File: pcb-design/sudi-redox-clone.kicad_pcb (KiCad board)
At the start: 2 copper layers, 204.9 x 155.4 mm, 110 parts, among them J1 RJ12_LEFT, J2 Serial_Out, J3 0.91 OLED, J4 RJ12_RIGHT, K1 KEYSW, K10 KEYSW, K11 KEYSW, K12 KEYSW, K13 KEYSW, K14 KEYSW, K15 KEYSW, K16 KEYSW, K17 KEYSW, K18 KEYSW, K19 KEYSW, K2 KEYSW, K20 KEYSW, K21 KEYSW, K22 KEYSW, K23 KEYSW, K24 KEYSW, K25 KEYSW, K26 KEYSW, K27 KEYSW, K28 KEYSW, K29 KEYSW, K3 KEYSW, K30 KEYSW, K31 KEYSW, K32 KEYSW, K33 KEYSW, K34 KEYSW, K35 KEYSW, K36 KEYSW, K37 KEYSW, K38 KEYSW, K39 KEYSW, K4 KEYSW, K40 KEYSW, K41 KEYSW, K42 KEYSW, K5 KEYSW, K6 KEYSW, K7 KEYSW, K8 KEYSW, K9 KEYSW, U1 ProMicro, U2 MCP23017_SP

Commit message: updatee
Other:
- board text added: "MAKE Front Back MCP23017 MAKE Front Back RJ12 Socket"
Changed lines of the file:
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@@
+		)
+	)
+	(gr_text "MAKE Front Back MCP23017\nMAKE Front Back RJ12 Socket"
+		(at 241 47.5 0)
+		(layer "User.1")
+		(effects
+			(font
+				(size 5 5)
+				(thickness 1.25)
+				(bold yes)
+			)
+			(justify left bottom)
 		)
 	)

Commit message: [minggu 7 juli 12:12] create pcb cut profile
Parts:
- removed D32, D33, D34, D35, D36, D37, D38, D39, D40, D41, D42: 1N5820, canadian_footprints:D_SOD123_axial-dual
- removed K19, K20, K21, K22, K23, K24, K25, K26, K27, K28, K29, K30, K31, K32, K33, K34, K35, K36, K37, K38, K39, K40, K41, K42: KEYSW, canadian_footprints:Mx_Alps_100-dualside
- added AE1: 2.4GHz, RF_Antenna:Texas_SWRA117D_2.4GHz_Left, F.Cu at (65.8, 92.2)
- added AE2: 2.4GHz, RF_Antenna:Texas_SWRA117D_2.4GHz_Left, F.Cu at (-27.0, -81.6)
- added C1: 10uF, Capacitor_SMD:C_0805_2012Metric_Pad1.18x1.45mm_HandSolder, F.Cu at (-52.9, -133.3)
- added C10: 1uF, Capacitor_SMD:C_0805_2012Metric_Pad1.18x1.45mm_HandSolder, F.Cu at (-61.3, -58.9)
- added C11: 100nF, Capacitor_SMD:C_0805_2012Metric_Pad1.18x1.45mm_HandSolder, F.Cu at (-52.9, -121.3)
- added C12: 47nF, Capacitor_SMD:C_0805_2012Metric_Pad1.18x1.45mm_HandSolder, F.Cu at (-52.9, -118.2)
- added C13: 100nF, Capacitor_SMD:C_0805_2012Metric_Pad1.18x1.45mm_HandSolder, F.Cu at (-48.1, -133.3)
- added C14: 1nF, Capacitor_SMD:C_0805_2012Metric_Pad1.18x1.45mm_HandSolder, F.Cu at (-48.1, -130.3)
- added C15: 2.2pF, Capacitor_SMD:C_0805_2012Metric_Pad1.18x1.45mm_HandSolder, F.Cu at (-48.1, -127.3)
- added C16: 1pF, Capacitor_SMD:C_0805_2012Metric_Pad1.18x1.45mm_HandSolder, F.Cu at (-48.1, -124.3)
- added C17: 1.5p, Capacitor_SMD:C_0805_2012Metric_Pad1.18x1.45mm_HandSolder, F.Cu at (-48.1, -121.3)
- added C18: 2.2nF, Capacitor_SMD:C_0805_2012Metric_Pad1.18x1.45mm_HandSolder, F.Cu at (-48.1, -118.2)
- added C19: 12pF, Capacitor_SMD:C_0805_2012Metric_Pad1.18x1.45mm_HandSolder, F.Cu at (-43.3, -133.3)
- added C2: 10uF/5V, Capacitor_SMD:C_0805_2012Metric_Pad1.18x1.45mm_HandSolder, F.Cu at (-52.9, -130.3)
- added C20: 12pF, Capacitor_SMD:C_0805_2012Metric_Pad1.18x1.45mm_HandSolder, F.Cu at (-43.3, -130.3)
- added C21: 100nF, Capacitor_SMD:C_0805_2012Metric_Pad1.18x1.45mm_HandSolder, F.Cu at (-43.3, -127.3)
- added C22: 10uF/5V, Capacitor_SMD:C_0805_2012Metric_Pad1.18x1.45mm_HandSolder, F.Cu at (-61.3, -55.9)
- added C23: 100nF, Capacitor_SMD:C_0805_2012Metric_Pad1.18x1.45mm_HandSolder, F.Cu at (-61.3, -52.9)
- added C24: 1.5p, Capacitor_SMD:C_0805_2012Metric_Pad1.18x1.45mm_HandSolder, F.Cu at (-56.5, -70.9)
- added C25: 1pF, Capacitor_SMD:C_0805_2012Metric_Pad1.18x1.45mm_HandSolder, F.Cu at (-56.5, -67.9)
- added C26: 2.2pF, Capacitor_SMD:C_0805_2012Metric_Pad1.18x1.45mm_HandSolder, F.Cu at (-56.5, -64.9)
- added C27: 2.2nF, Capacitor_SMD:C_0805_2012Metric_Pad1.18x1.45mm_HandSolder, F.Cu at (-56.5, -61.9)
- added C28: 12pF, Capacitor_SMD:C_0805_2012Metric_Pad1.18x1.45mm_HandSolder, F.Cu at (-56.5, -58.9)
- added C29: 12pF, Capacitor_SMD:C_0805_2012Metric_Pad1.18x1.45mm_HandSolder, F.Cu at (-56.5, -55.9)
- added C3: 10uF/5V, Capacitor_SMD:C_0805_2012Metric_Pad1.18x1.45mm_HandSolder, F.Cu at (-52.9, -127.3)
- added C30: 47nF, Capacitor_SMD:C_0805_2012Metric_Pad1.18x1.45mm_HandSolder, F.Cu at (-56.5, -52.9)
- added C31: 100nF, Capacitor_SMD:C_0805_2012Metric_Pad1.18x1.45mm_HandSolder, F.Cu at (-51.7, -70.9)
- added C32: 100nF, Capacitor_SMD:C_0805_2012Metric_Pad1.18x1.45mm_HandSolder, F.Cu at (-51.7, -67.9)
- added C33: 100nF, Capacitor_SMD:C_0805_2012Metric_Pad1.18x1.45mm_HandSolder, F.Cu at (-51.7, -64.9)
- added C34: 1nF, Capacitor_SMD:C_0805_2012Metric_Pad1.18x1.45mm_HandSolder, F.Cu at (-51.7, -61.9)
- added C4: 10uF, Capacitor_SMD:C_0805_2012Metric_Pad1.18x1.45mm_HandSolder, F.Cu at (-52.9, -124.3)
- added C5: 22pF, Capacitor_SMD:C_0805_2012Metric_Pad1.18x1.45mm_HandSolder, F.Cu at (-61.3, -70.9)
- added C6: 22pF, Capacitor_SMD:C_0805_2012Metric_Pad1.18x1.45mm_HandSolder, F.Cu at (-61.3, -67.9)
- added C7: 100nF, Capacitor_SMD:C_0805_2012Metric_Pad1.18x1.45mm_HandSolder, F.Cu at (-61.3, -64.9)
- added C9: 10uF/5V, Capacitor_SMD:C_0805_2012Metric_Pad1.18x1.45mm_HandSolder, F.Cu at (-61.3, -61.9)
- added D43: WS2812B, LED_SMD:LED_WS2812B_PLCC4_5.0x5.0mm_P3.2mm, F.Cu at (-59.5, -131.5)
- added D44: WS2812B, LED_SMD:LED_WS2812B_PLCC4_5.0x5.0mm_P3.2mm, F.Cu at (-59.5, -124.9)
- added D45: WS2812B, LED_SMD:LED_WS2812B_PLCC4_5.0x5.0mm_P3.2mm, F.Cu at (-59.5, -118.3)
- added D46: WS2812B, LED_SMD:LED_WS2812B_PLCC4_5.0x5.0mm_P3.2mm, F.Cu at (-59.5, -111.6)
- added D47: WS2812B, LED_SMD:LED_WS2812B_PLCC4_5.0x5.0mm_P3.2mm, F.Cu at (-59.5, -105.0)
- added D48: WS2812B, LED_SMD:LED_WS2812B_PLCC4_5.0x5.0mm_P3.2mm, F.Cu at (-59.5, -98.4)
- added FB1: 60R@100Mhz, Inductor_SMD:L_0603_1608Metric_Pad1.05x0.95mm_HandSolder, F.Cu at (-53.1, -99.0)
- added FB2: 60R@100Mhz, Inductor_SMD:L_0603_1608Metric_Pad1.05x0.95mm_HandSolder, F.Cu at (-26.7, -71.2)
- added J10: ARM_JTAG, Connector_PinHeader_1.27mm:PinHeader_2x05_P1.27mm_Vertical, F.Cu at (-47.1, -57.5)
- added J6: USB_A, Connector_USB:USB_A_CNCTech_1001-011-01101_Horizontal, F.Cu at (61.2, 74.1)
- added J7: ARMJTAG, Connector_PinHeader_2.54mm:PinHeader_2x05_P2.54mm_Horizontal, F.Cu at (-47.3, -114.4)
- added J8: BatCon, Connector_PinHeader_2.54mm:PinHeader_1x02_P2.54mm_Horizontal, F.Cu at (-47.3, -99.6)
- added J9: AVR-ISP-6, Connector_PinHeader_2.54mm:PinHeader_2x05_P2.54mm_Vertical, F.Cu at (56.6, 106.9)
- added L1: 10nH, Inductor_SMD:L_0603_1608Metric_Pad1.05x0.95mm_HandSolder, F.Cu at (-53.1, -96.5)
- added L2: 4.7nH, Inductor_SMD:L_0603_1608Metric_Pad1.05x0.95mm_HandSolder, F.Cu at (-53.1, -94.0)
- added L3: 3.3nH, Inductor_SMD:L_0603_1608Metric_Pad1.05x0.95mm_HandSolder, F.Cu at (-53.1, -91.5)
- added L4: 3.3nH, Inductor_SMD:L_0603_1608Metric_Pad1.05x0.95mm_HandSolder, F.Cu at (-26.7, -68.7)
- added L5: 10nH, Inductor_SMD:L_0603_1608Metric_Pad1.05x0.95mm_HandSolder, F.Cu at (-26.7, -66.2)
- added L6: 4.7nH, Inductor_SMD:L_0603_1608Metric_Pad1.05x0.95mm_HandSolder, F.Cu at (-26.7, -63.7)
- added R3: 5K1, Resistor_SMD:R_1206_3216Metric, F.Cu at (-52.5, -115.1)
- added R4: 5K1, Resistor_SMD:R_1206_3216Metric, F.Cu at (-52.5, -111.8)
- added R5: 1K, Resistor_SMD:R_1206_3216Metric, F.Cu at (-52.5, -108.5)
- added R6: 1K, Resistor_SMD:R_1206_3216Metric, F.Cu at (-52.5, -105.2)
- added R7: 1.2, Resistor_SMD:R_1206_3216Metric, F.Cu at (-52.5, -101.9)
- added R8: 1K, Resistor_SMD:R_1206_3216Metric, F.Cu at (-41.0, -57.5)
- added R9: 1K, Resistor_SMD:R_1206_3216Metric, F.Cu at (-41.0, -54.2)
- added SW2: RCV_RST, Button_Switch_SMD:SW_Push_1P1T_NO_6x6mm_H9.5mm, F.Cu at (-30.6, -53.9)
- added U3: nRF51x22-QFxx, Package_DFN_QFN:QFN-48-1EP_6x6mm_P0.4mm_EP4.6x4.6mm, F.Cu at (-35.7, -76.6)
- added U4: AMS1117-3.3, Package_TO_SOT_SMD:SOT-223-3_TabPin2, F.Cu at (-35.9, -123.5)
- added U5: nRF51x22-QFxx, Package_DFN_QFN:QFN-48-1EP_6x6mm_P0.4mm_EP4.6x4.6mm, F.Cu at (-29.6, -93.9)
- added U6: TP4056, Package_SO:SOIC-8-1EP_3.9x4.9mm_P1.27mm_EP2.29x3mm, F.Cu at (-26.8, -124.3)
- added U8: MCP23017_SS, Package_SO:SSOP-28_5.3x10.2mm_P0.65mm, F.Cu at (-28.4, -104.1)
- added Y2: 16MHz, Crystal:Crystal_HC50_Vertical, F.Cu at (-29.6, -113.4)
- added Y3: 16MHz, Crystal:Crystal_HC50_Vertical, F.Cu at (-45.1, -69.1)
- added Y4: 8MHz, Crystal:Crystal_HC50_Vertical, F.Cu at (-45.1, -62.5)
- D10, D11, D12, D16, D17, D18, D22, D23, D24, D28, D5, D6: value 1N5820 -> WS2812B; footprint canadian_footprints:D_SOD123_axial-dual -> LED_SMD:LED_WS2812B_PLCC4_5.0x5.0mm_P3.2mm
- D4: value 1N5820 -> RED; footprint canadian_footprints:D_SOD123_axial-dual -> LED_SMD:LED_0805_2012Metric_Pad1.15x1.40mm_HandSolder
- J1: footprint Connector_RJ:RJ12_Amphenol_54601 -> Connector_RJ:RJ25_Wayconn_MJEA-660X1_Horizontal
- J2: value Serial_Out -> 0.91 OLED; footprint Connector_PinHeader_2.54mm:PinHeader_1x03_P2.54mm_Horizontal -> Connector_PinHeader_2.54mm:PinHeader_1x04_P2.54mm_Vertical; moved to F.Cu
- J3: value 0.91 OLED -> RJ12_RIGHT; footprint KiCad-SSD1306-0.91-OLED-4pin-128x32:SSD1306-0.91-OLED-4pin-128x32 -> Connector_RJ:RJ25_Wayconn_MJEA-660X1_Horizontal
- J4: value RJ12_RIGHT -> USBC_PWR_ONLY; footprint Connector_RJ:RJ12_Amphenol_54601 -> Connector_USB:USB_C_Receptacle_GCT_USB4125-xx-x-0190_6P_TopMnt_Horizontal
- K2, K3, K4: footprint canadian_footprints:Mx_Alps_150-dualsided -> canadian_footprints:Mx_Alps_100-dualside
- U1: value ProMicro -> AMS1117-3.3; footprint canadian_footprints:Pro_Micro -> Package_TO_SOT_SMD:SOT-223-3_TabPin2
- U2: value MCP23017_SP -> ATmega8U2-A; footprint Package_DIP:DIP-28_W7.62mm -> Package_QFP:TQFP-32_7x7mm_P0.8mm
- moved D10 191.9 mm to (103.1, -158.2)
- moved D15 191.9 mm to (123.4, -164.5)
- moved D17 191.9 mm to (123.4, -125.1)
- moved D19 191.9 mm to (123.4, -84.5)
- moved D2 191.9 mm to (57.4, -120.1)
- moved D23 191.9 mm to (143.7, -102.3)
- moved D25 191.9 mm to (164.1, -158.2)
- moved D28 191.9 mm to (164.1, -97.2)
- moved D31 191.9 mm to (184.4, -132.8)
- moved D4 191.9 mm to (57.4, -79.4)
- moved D6 191.9 mm to (82.8, -132.8)
- moved D7 191.9 mm to (82.8, -111.2)
- moved FID8 191.9 mm to (230.1, -59.1)
- moved FID9 191.9 mm to (70.1, -106.1)
- moved H2 191.9 mm to (222.1, -133.1)
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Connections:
- D10 pad 1: row4 -> +3V7
- D10 pad 2: Net-(D10-A) -> Net-(D10-DOUT)
- D11 pad 1: row5 -> +3V7
- D11 pad 2: Net-(D11-A) -> Net-(D11-DOUT)
- D12 pad 1: row6 -> +3V7
- D12 pad 2: Net-(D12-A) -> Net-(D12-DOUT)
- D16 pad 1: row4 -> +3V7
- D16 pad 2: Net-(D16-A) -> Net-(D16-DOUT)
- D17 pad 1: row5 -> +3V7
- D17 pad 2: Net-(D17-A) -> Net-(D17-DOUT)
- D18 pad 1: row6 -> +3V7
- D18 pad 2: Net-(D18-A) -> Net-(D18-DOUT)
- D22 pad 1: row4 -> +3V7
- D22 pad 2: Net-(D22-A) -> Net-(D22-DOUT)
- D23 pad 1: row5 -> +3V7
- D23 pad 2: Net-(D23-A) -> Net-(D23-DOUT)
- D24 pad 1: row6 -> +3V7
- D24 pad 2: Net-(D24-A) -> Net-(D24-DOUT)
- D28 pad 1: row4 -> +3V7
- D28 pad 2: Net-(D28-A) -> unconnected-(D28-DOUT-Pad2)
- D29 pad 1: row5 -> row1
- D30 pad 1: row6 -> row2
- D31 pad 1: row1 -> row3
- D4 pad 1: row4 -> Net-(D4-K)
- D4 pad 2: Net-(D4-A) -> +5V
- D5 pad 1: row5 -> +3V7
- D5 pad 2: Net-(D5-A) -> Net-(D5-DOUT)
- D6 pad 1: row6 -> +3V7
- D6 pad 2: Net-(D6-A) -> Net-(D10-DIN)
- H2 pad 1: GND -> unconnected-(H2-Pad1)
- H8 pad 1: unconnected-(H8-Pad1) -> GND
- J1 pad 1: unconnected-(J1-Pad1) -> GND
- J1 pad 2: GND -> Tx
- J1 pad 3: Tx -> SCL
- J1 pad 4: SCL -> SDA
- J1 pad 5: SDA -> +3V7
- J2 pad 1: +5V -> GND
- J2 pad 2: Tx -> +3V7
- J2 pad 3: GND -> SCL
- J3 pad 2: +5V -> Tx
- K10 pad 1: col2 -> col4
- K10 pad 2: Net-(D10-A) -> Net-(D19-A)
- K11 pad 1: col2 -> col4
- K11 pad 2: Net-(D11-A) -> Net-(D20-A)
- K12 pad 1: col2 -> col4
- K12 pad 2: Net-(D12-A) -> Net-(D21-A)
- K13 pad 1: col3 -> col5
- K13 pad 2: Net-(D13-A) -> Net-(D25-A)
- K14 pad 1: col3 -> col5
- K14 pad 2: Net-(D14-A) -> Net-(D26-A)
- K15 pad 1: col3 -> col5
- K15 pad 2: Net-(D15-A) -> Net-(D27-A)
- K16 pad 1: col3 -> col6
- K16 pad 2: Net-(D16-A) -> Net-(D29-A)
- K17 pad 1: col3 -> col6
- K17 pad 2: Net-(D17-A) -> Net-(D30-A)
- K18 pad 1: col3 -> col6
- K18 pad 2: Net-(D18-A) -> Net-(D31-A)
- K4 pad 1: col1 -> col2
- K4 pad 2: Net-(D4-A) -> Net-(D7-A)
- K5 pad 1: col1 -> col2
- K5 pad 2: Net-(D5-A) -> Net-(D8-A)
- K6 pad 1: col1 -> col2
- K6 pad 2: Net-(D6-A) -> Net-(D9-A)
- K7 pad 1: col2 -> col3
- K7 pad 2: Net-(D7-A) -> Net-(D13-A)
- K8 pad 1: col2 -> col3
- K8 pad 2: Net-(D8-A) -> Net-(D14-A)
- K9 pad 1: col2 -> col3
- K9 pad 2: Net-(D9-A) -> Net-(D15-A)
- R1 pad 1: +5V -> +3.3V
- R2 pad 1: +5V -> +3.3V
- U1 pad 1: unconnected-(U1-RAW-Pad1) -> GND
- U1 pad 2: GND -> +3.3V
- U1 pad 3: unconnected-(U1-RST-Pad3) -> +5V
- U2 pad 1: col1 -> Net-(U2-XTAL1)
- U2 pad 10: GND -> unconnected-(U2-PD4-Pad10)
- U2 pad 12: SCL -> unconnected-(U2-PD6-Pad12)
- U2 pad 13: SDA -> unconnected-(U2-~{HWB}/PD7-Pad13)
- U2 pad 15: GND -> /Receiver/RCV_SCK
- U2 pad 16: +5V -> /Receiver/RCV_MOSI
- U2 pad 17: +5V -> /Receiver/RCV_MISO
- U2 pad 18: +5V -> unconnected-(U2-PB4-Pad18)
- U2 pad 2: col2 -> Net-(U2-PC0/XTAL2)
- U2 pad 21: row1 -> unconnected-(U2-PB7-Pad21)
- U2 pad 22: row2 -> unconnected-(U2-PC7-Pad22)
- U2 pad 23: row3 -> unconnected-(U2-PC6-Pad23)
- U2 pad 24: row4 -> /Receiver/RCV_RST
- U2 pad 25: row5 -> unconnected-(U2-PC5-Pad25)
- U2 pad 26: row6 -> unconnected-(U2-PC4-Pad26)
- U2 pad 27: unconnected-(U2-GPA6-Pad27) -> Net-(U2-UCAP)
- U2 pad 28: unconnected-(U2-GPA7-Pad28) -> GND
- U2 pad 3: col3 -> GND
- U2 pad 4: col4 -> +3.3V
- U2 pad 5: col5 -> unconnected-(U2-PC2-Pad5)
- U2 pad 6: col6 -> unconnected-(U2-PD0-Pad6)
- U2 pad 7: col7 -> unconnected-(U2-PD1-Pad7)
- U2 pad 8: unconnected-(U2-GPB7-Pad8) -> /Receiver/RCV_USART1_RX
- U2 pad 9: +5V -> /Receiver/RCV_USART1_TX
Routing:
- net row4: track 565.9 -> 0.00 mm, vias 30 -> 0
- net row2: track 546.5 -> 0.00 mm, vias 30 -> 0
- net row3: track 527.4 -> 0.00 mm, vias 27 -> 0
- net row5: track 494.7 -> 0.00 mm, vias 26 -> 0
- net row1: track 457.3 -> 0.00 mm, vias 30 -> 0
- net row6: track 441.8 -> 0.00 mm, vias 30 -> 0
- net col1: track 371.1 -> 0.00 mm, vias 1 -> 0
- net col2: track 339.5 -> 0.00 mm, vias 1 -> 0
- net col7: track 330.0 -> 0.00 mm, vias 3 -> 0
- net col6: track 295.0 -> 0.00 mm, vias 1 -> 0
- net col3: track 293.7 -> 0.00 mm, vias 3 -> 0
- net col4: track 278.2 -> 0.00 mm, vias 1 -> 0
- net col5: track 278.2 -> 0.00 mm, vias 1 -> 0
- net SDA: track 253.2 -> 0.00 mm, vias 3 -> 0
- net SCL: track 243.0 -> 0.00 mm, vias 1 -> 0
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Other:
- board size 204.9 x 155.4 mm -> 141.8 x 94.5 mm

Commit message: [minggu 7 juli 19:32] finish PCB Layout
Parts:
- removed H1, H2: MountingHole_Pad, MountingHole:MountingHole_3.2mm_M3_DIN965_Pad
- C1, C11, C12, C13, C14, C2, C21, C24, C25, C26, C27, C28, C29, C3, C30, C31, C32, C33, C34, C4, D4, FB1, FB2, FID6, J3, J7, J8, L4, L5, L6, SW2, U1, U6, U8, Y4: moved to B.Cu
- D10, D11, D12, D16, D17, D18, D22, D23, D24, D28, D43, D44, D45, D46, D47, D48, D5, D6: footprint LED_SMD:LED_WS2812B_PLCC4_5.0x5.0mm_P3.2mm -> CustomWS2185BFootPrint:LED_WS2812B_PLCC4_5.0x5.0mm_P3.2mm; moved to B.Cu
- J4: moved to F.Cu
- K1, K10, K11, K12, K13, K14, K15, K16, K17, K18, K2, K3, K4, K5, K6, K7, K8, K9: footprint canadian_footprints:Mx_Alps_100-dualside -> keyswitches.pretty-master:Kailh_socket_MX_optional_reversible_platemount
- R1, R2: footprint Resistor_SMD:R_1206_3216Metric -> Resistor_SMD:R_0805_2012Metric_Pad1.20x1.40mm_HandSolder; moved to F.Cu
- R3, R4, R5, R6, R7: footprint Resistor_SMD:R_1206_3216Metric -> Resistor_SMD:R_0805_2012Metric_Pad1.20x1.40mm_HandSolder; moved to B.Cu
- R8, R9: footprint Resistor_SMD:R_1206_3216Metric -> Resistor_SMD:R_0805_2012Metric_Pad1.20x1.40mm_HandSolder
- moved D48 349.0 mm to (187.3, 148.4), turned to 180 degrees
- moved C19 338.6 mm to (180.6, 120.7), turned to 90 degrees
- moved C20 338.3 mm to (183.6, 120.7), turned to 90 degrees
- moved C3 334.4 mm to (184.4, 108.3), turned to 90 degrees
- moved C13 333.4 mm to (185.8, 104.3), turned to 90 degrees
- moved C2 330.6 mm to (176.0, 108.3), turned to 90 degrees
- moved C14 329.1 mm to (182.8, 104.3), turned to 90 degrees
- moved C21 327.7 mm to (188.5, 104.4), turned to 90 degrees
- moved C18 325.8 mm to (189.9, 104.3), turned to 90 degrees
- moved C17 325.7 mm to (186.9, 104.3), turned to 90 degrees
- moved C16 325.6 mm to (183.9, 104.3), turned to 90 degrees
- moved C15 325.6 mm to (180.9, 104.3), turned to 90 degrees
- moved R5 325.1 mm to (178.2, 120.6), turned to 90 degrees
- moved C11 324.2 mm to (180.1, 104.2), turned to 90 degrees
- moved R3 323.8 mm to (181.9, 108.3), turned to 90 degrees
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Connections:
- H8 pad 1: GND -> unconnected-(H8-Pad1)
- H9 pad 1: GND -> unconnected-(H9-Pad1)
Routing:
- removed copper zone on F.Cu, net +5V
- removed copper zone on B.Cu, net GND
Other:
- board size 141.8 x 94.5 mm -> 141.8 x 99.4 mm
- board text added: "9 November 2023 7 Juli 2024"
- board text added: "AHAH_TERROR 7_JULY_2024"
- board text added: "REGIROCK"
- board text added: "SUDI V2"
- board text removed: "9 November 2023"
- board text removed: "AHAH_TERROR NOV_2023"
- board text removed: "SUDI"
- board text removed: "Sudden Unexpected Death Instant"

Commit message: add some route progress
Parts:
- turned D20 to 0 degrees
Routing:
- net row1: track 0.00 -> 157.9 mm
- net row2: track 0.00 -> 135.2 mm
- net row3: track 0.00 -> 130.4 mm, vias 0 -> 1
- net Net-(D14-A): track 0.00 -> 23.8 mm
- net Net-(D25-A): track 0.00 -> 23.7 mm
- net Net-(D30-A): track 0.00 -> 23.0 mm
- net Net-(D8-A): track 0.00 -> 22.9 mm
- net Net-(D31-A): track 0.00 -> 22.8 mm
- net Net-(D27-A): track 0.00 -> 22.6 mm
- net Net-(D26-A): track 0.00 -> 22.5 mm
- net Net-(D7-A): track 0.00 -> 22.4 mm
- net Net-(D15-A): track 0.00 -> 22.3 mm
- net Net-(D13-A): track 0.00 -> 22.3 mm
- net Net-(D21-A): track 0.00 -> 22.3 mm
- net Net-(D20-A): track 0.00 -> 22.2 mm
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
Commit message: update some route
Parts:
- moved J3 8.41 mm to (191.6, 68.9)
- moved D10 0.27 mm to (132.7, 80.8)
- moved D22 0.21 mm to (132.8, 100.5)
- moved D43 0.20 mm to (94.1, 75.0)
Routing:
- net GND: track 0.00 -> 290.6 mm, vias 0 -> 16
- net +3V7: track 0.00 -> 105.3 mm, vias 0 -> 8
- net col1: track 0.00 -> 55.6 mm, vias 0 -> 3
- net col5: track 0.00 -> 36.6 mm, vias 0 -> 1
- net col4: track 0.00 -> 36.6 mm
- net col6: track 0.00 -> 36.6 mm, vias 0 -> 1
- net Net-(U5-VDD_PA): track 0.00 -> 36.2 mm, vias 0 -> 2
- net /SWDIO: track 0.00 -> 35.9 mm, vias 0 -> 1
- net +3.3V: track 0.00 -> 34.3 mm, vias 0 -> 4
- net Net-(U5-ANT1): track 0.00 -> 34.2 mm, vias 0 -> 2
- net Net-(U5-ANT2): track 0.00 -> 25.0 mm, vias 0 -> 2
- net Net-(U5-DEC2): track 0.00 -> 21.9 mm, vias 0 -> 3
- net /SWCLK: track 0.00 -> 19.4 mm, vias 0 -> 4
- net col3: track 0.00 -> 12.2 mm
- net Net-(U5-XC1): track 0.00 -> 10.4 mm
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
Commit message: [rabu 17 juli 19:13] update route progress
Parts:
- C19, C20: moved to B.Cu
- moved J3 3.14 mm to (190.5, 71.8)
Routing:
- net row1: track 157.9 -> 316.9 mm, vias 0 -> 4
- net col2: track 0.00 -> 149.4 mm, vias 0 -> 5
- net /USART1_TX: track 0.00 -> 136.0 mm, vias 0 -> 4
- net col1: track 55.6 -> 183.4 mm, vias 3 -> 8
- net col3: track 12.2 -> 136.0 mm, vias 0 -> 4
- net row2: track 131.0 -> 251.3 mm, vias 1 -> 6
- net col5: track 36.6 -> 139.9 mm, vias 1 -> 7
- net row3: track 130.4 -> 218.4 mm, vias 1 -> 6
- net col4: track 36.6 -> 115.6 mm, vias 0 -> 4
- net col6: track 36.6 -> 106.7 mm, vias 1 -> 6
- net GND: track 290.6 -> 333.1 mm, vias 16 -> 20
- net +5V: track 3.35 -> 11.4 mm
- net Net-(D16-DOUT): track 0.00 -> 5.48 mm, vias 0 -> 1
- net Net-(D17-DOUT): track 0.00 -> 4.90 mm, vias 0 -> 1

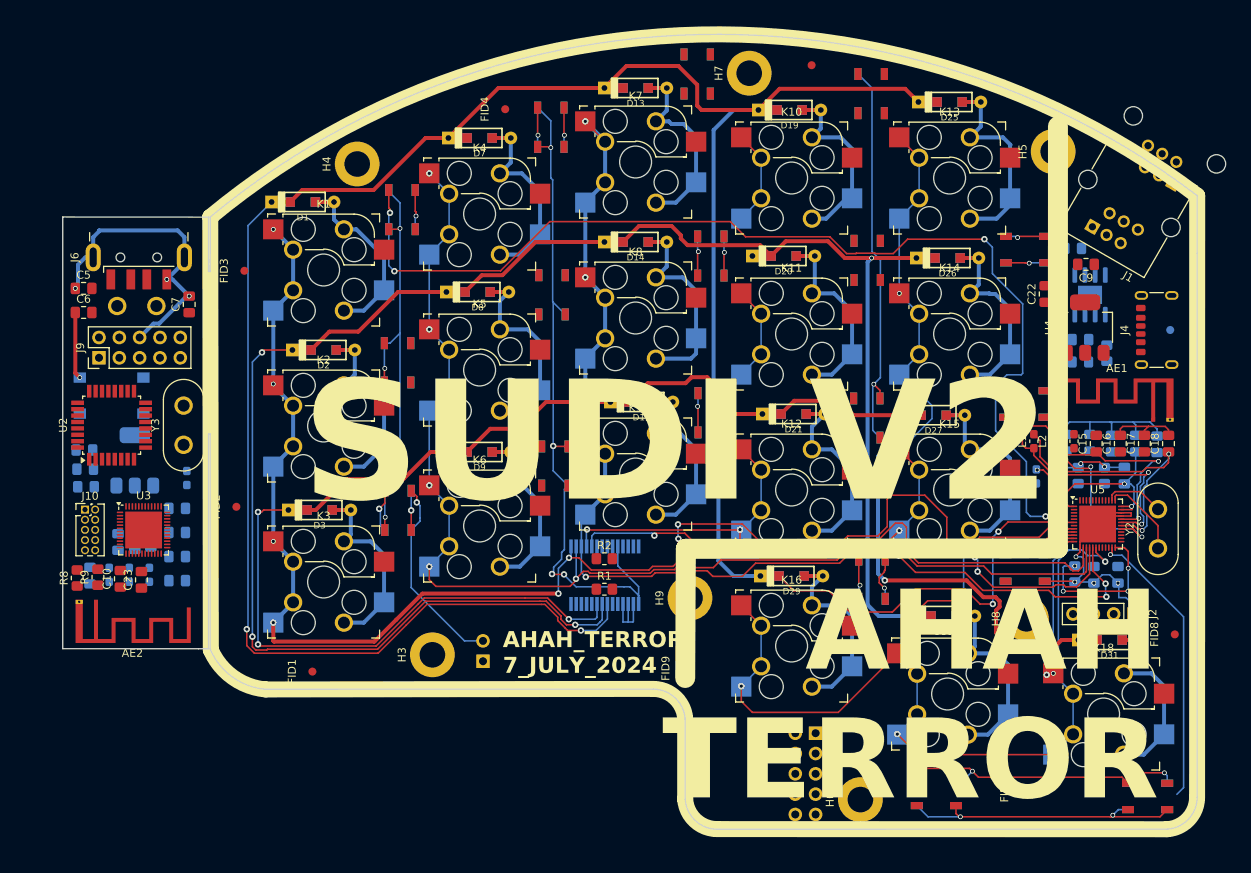
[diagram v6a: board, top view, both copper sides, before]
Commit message: [rabu 24 juli 20:17] finish keyboard layout - todo receiver
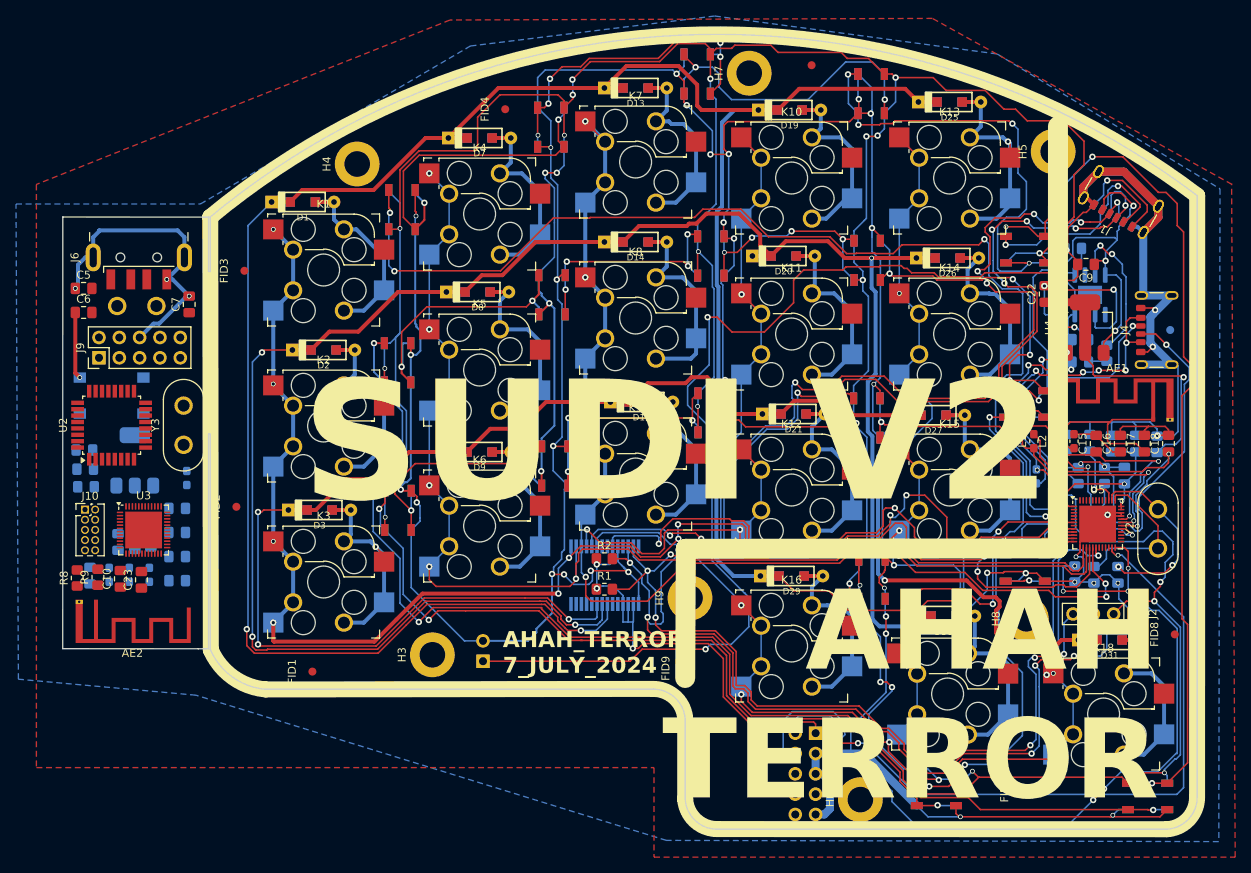
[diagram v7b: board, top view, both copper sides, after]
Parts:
- removed J3: RJ12_RIGHT, Connector_RJ:RJ25_Wayconn_MJEA-660X1_Horizontal
- added J5: SIDE_CON, Connector_USB:USB_C_Receptacle_GCT_USB4125-xx-x-0190_6P_TopMnt_Horizontal, B.Cu at (184.5, 73.2)
- J1: value RJ12_LEFT -> SIDE_CON; footprint Connector_RJ:RJ25_Wayconn_MJEA-660X1_Horizontal -> Connector_USB:USB_C_Receptacle_GCT_USB4125-xx-x-0190_6P_TopMnt_Horizontal
- moved J1 5.77 mm to (184.5, 73.2)
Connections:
- U8 pad 16: +5V -> +3.3V
- U8 pad 17: +5V -> +3.3V
- U8 pad 18: +5V -> +3.3V
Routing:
- net +3V7: track 105.3 -> 565.5 mm, vias 8 -> 31
- net GND: track 333.1 -> 738.8 mm, vias 20 -> 55
- net SCL: track 0.00 -> 222.7 mm, vias 0 -> 13
- net SDA: track 0.00 -> 212.5 mm, vias 0 -> 13
- net +3.3V: track 34.3 -> 194.0 mm, vias 4 -> 10
- net Net-(D48-DOUT): track 0.00 -> 150.0 mm, vias 0 -> 3
- net Net-(J8-Pin_1): track 0.00 -> 134.6 mm, vias 0 -> 3
- net Net-(D47-DOUT): track 5.02 -> 112.2 mm, vias 1 -> 4
- net /SWCLK: track 19.4 -> 114.1 mm, vias 4 -> 8
- net Net-(D16-DOUT): track 5.48 -> 99.9 mm, vias 1 -> 3
- net Net-(D12-DOUT): track 0.00 -> 68.2 mm, vias 0 -> 4
- net +5V: track 11.4 -> 78.7 mm, vias 2 -> 7
- net /SWDIO: track 35.9 -> 90.9 mm, vias 1 -> 3
- net Net-(D46-DOUT): track 4.94 -> 58.4 mm, vias 1 -> 4
- net Net-(D23-DOUT): track 0.00 -> 48.3 mm, vias 0 -> 3
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- added copper zone on F.Cu, net +3.3V
- added copper zone on B.Cu, net GND
